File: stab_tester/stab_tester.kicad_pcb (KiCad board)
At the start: 2 copper layers, 119.6 x 68 mm, 6 parts

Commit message: update stabilizer tester pcb
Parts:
- removed the REF** at (101.6, 163.0) (x2)
- moved REF** 5.44 mm to (101.5, 151.5)
- moved REF** 3.68 mm to (74.5, 129.9) (x2)
- moved REF** 3.68 mm to (127.6, 129.9)
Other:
- board size 119.6 x 68 mm -> 109.5 x 58 mm

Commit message: update stab tester
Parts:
- moved REF** 218.4 mm to (264.9, 23.1) (x2)
- moved REF** 81.9 mm to (65.9, 77.8)
- moved REF** 54.1 mm to (142.1, 77.8)
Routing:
- removed copper zone on B.Cu, net (none)
- removed copper zone on F.Cu, net (none)
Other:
- board size 109.5 x 58 mm -> 105.9 x 14.1 mm
- board text added: "+- 0"

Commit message: Footprint should be correct
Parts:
- removed the REF** at (264.9, 23.1) (x2)
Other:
- board size 105.9 x 14.1 mm -> 106 x 14.9 mm
- board text removed: "+- 0"

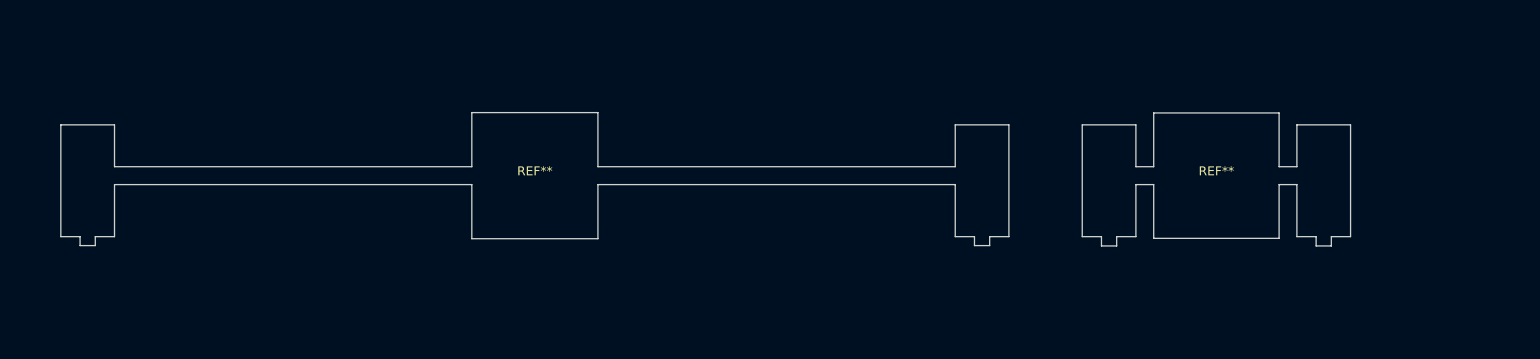
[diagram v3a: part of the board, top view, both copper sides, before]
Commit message: Fix stab footprint
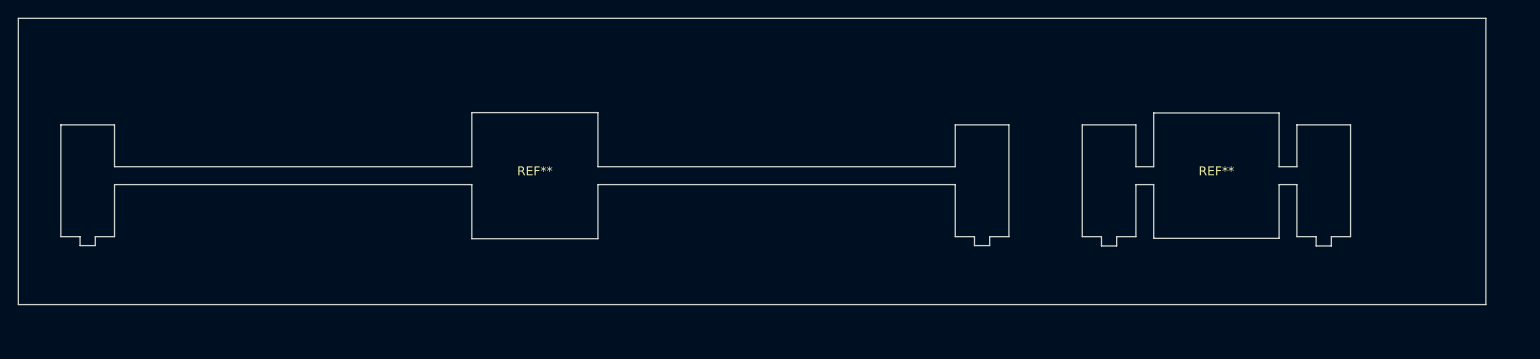
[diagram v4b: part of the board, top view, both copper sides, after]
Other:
- board size 106 x 14.9 mm -> 164.1 x 32 mm
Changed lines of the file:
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@@
       (pts (xy 154.08125 72.2075) (xy 130.08125 72.2075))
       (height 7.881999)
-      (gr_text "0.9449 in" (at 142.08125 63.175501) (layer "F.SilkS")
+      (gr_text "24.0000 mm" (at 142.08125 63.175501) (layer "F.SilkS")
         (effects (font (size 1 1) (thickness 0.15)))
       )
@@
       (pts (xy 157.08125 84.608) (xy 157.08125 72.108))
       (height 4.0754)
-      (gr_text "0.4921 in" (at 160.00665 78.358 90) (layer "F.SilkS")
+      (gr_text "12.5000 mm" (at 160.00665 78.358 90) (layer "F.SilkS")
         (effects (font (size 1 1) (thickness 0.15)))
       )
@@
   (gr_rect (start 100.0125 48.186234) (end 138.1125 67.236234)
     (stroke (width 0.15) (type default)) (fill none) (layer "Cmts.User"))
+  (gr_rect (start 8.128 60.198) (end 172.212 92.202)
+    (stroke (width 0.1) (type default)) (fill none) (layer "Edge.Cuts"))
   (dimension (type aligned) (layer "F.SilkS")
     (pts (xy 118.88125 84.608) (xy 118.88125 72.108))

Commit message: update stab tester pbc
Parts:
- added REF**: Gateron KS33 Plate, JohnDeereLibrary:Gateron KS33 Plate, F.Cu at (115.6, 124.5)
- added REF**: Gateron KS33 Plate, JohnDeereLibrary:Gateron KS33 Plate, F.Cu at (163.8, 124.5)
- added REF**: Gateron KS33 Plate, JohnDeereLibrary:Gateron KS33 Plate, F.Cu at (139.7, 124.5)
- added REF**: Gateron KS33 Plate, JohnDeereLibrary:Gateron KS33 Plate, F.Cu at (43.2, 104.1)
- added REF**: Gateron KS33 Plate, JohnDeereLibrary:Gateron KS33 Plate, F.Cu at (43.2, 144.8)
- added REF**: Gateron KS33 Plate, JohnDeereLibrary:Gateron KS33 Plate, F.Cu at (115.6, 104.1)
- added REF**: Gateron KS33 Plate, JohnDeereLibrary:Gateron KS33 Plate, F.Cu at (67.3, 144.8)
- added REF**: Gateron KS33 Plate, JohnDeereLibrary:Gateron KS33 Plate, F.Cu at (91.4, 144.8)
- added REF**: Gateron KS33 Plate, JohnDeereLibrary:Gateron KS33 Plate, F.Cu at (20.3, 104.1)
- added REF**: Gateron KS33 Plate, JohnDeereLibrary:Gateron KS33 Plate, F.Cu at (115.6, 144.8)
- added REF**: Gateron KS33 Plate, JohnDeereLibrary:Gateron KS33 Plate, F.Cu at (91.4, 124.5)
- added REF**: Gateron KS33 Plate, JohnDeereLibrary:Gateron KS33 Plate, F.Cu at (67.3, 124.5)
- added REF**: Gateron KS33 Plate, JohnDeereLibrary:Gateron KS33 Plate, F.Cu at (139.7, 144.8)
- added REF**: Gateron KS33 Plate, JohnDeereLibrary:Gateron KS33 Plate, F.Cu at (163.8, 144.8)
- added REF**: Gateron KS33 Plate, JohnDeereLibrary:Gateron KS33 Plate, F.Cu at (139.7, 104.1)
- added REF**: Gateron KS33 Plate, JohnDeereLibrary:Gateron KS33 Plate, F.Cu at (20.3, 124.5)
- added REF**: Gateron KS33 Plate, JohnDeereLibrary:Gateron KS33 Plate, F.Cu at (67.3, 104.1)
- added REF**: Gateron KS33 Plate, JohnDeereLibrary:Gateron KS33 Plate, F.Cu at (91.4, 104.1)
- added REF**: Gateron KS33 Plate, JohnDeereLibrary:Gateron KS33 Plate, F.Cu at (43.2, 124.5)
- added REF**: Gateron KS33 Plate, JohnDeereLibrary:Gateron KS33 Plate, F.Cu at (20.3, 144.8)
- added REF**: Gateron KS33 Plate, JohnDeereLibrary:Gateron KS33 Plate, F.Cu at (163.8, 104.1)
- moved REF** 5.18 mm to (69.0, 81.9)
- moved REF** 5.18 mm to (145.2, 81.9)
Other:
- board size 164.1 x 32 mm -> 162.6 x 88.9 mm
- board text added: "14.10 14.05 14.00 13.95 13.9 13.85 13.8"
